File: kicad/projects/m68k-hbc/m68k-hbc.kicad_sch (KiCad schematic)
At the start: 0 parts

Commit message: Modified system architecture, New KiCad Project: Cache Memory Module(SIMM80)
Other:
- removed sheet DMAC
- removed sheet DRAM
- added sheet Clock (Clock.kicad_sch)
- added sheet PBC (PBC.kicad_sch)
- added sheet SYSCON (SYSCON.kicad_sch)
- added sheet USB (USB.kicad_sch)

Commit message: Some Updates
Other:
- sheet EISA renamed ISA
- sheet PBC renamed SBC
- sheet SYSCON renamed CDC
- removed sheet ADDEC
- removed sheet Disk
- removed sheet IO
- removed sheet PIC
- added sheet ATA (ATA.kicad_sch)
- added sheet Config (Config.kicad_sch)
- added sheet DECAP (DECAP.kicad_sch)
- added sheet FDC (FDC.kicad_sch)
- added sheet I2C (I2C.kicad_sch)
- added sheet IO_Timer (IO_Timer.kicad_sch)
- added sheet KeyboardMouse (KeyboardMouse.kicad_sch)
- added sheet OPB (OPB.kicad_sch)
- added sheet PU_PD (PU_PD.kicad_sch)
- added sheet SPI (SPI.kicad_sch)
- sheet Audio ports: added DACK_ACC, DACK_ACP, DRQ_ACC, DRQ_ACP, IRQ_ACODEC, OPB, ~{CS_ACODEC}; removed none
- sheet CDC: file SYSCON.kicad_sch -> CDC.kicad_sch
- sheet CDC ports: added Local Bus, ~{RST_CDC}; removed none
- sheet CPU_FPU ports: added CPUCLK, FPUCLK, Local Bus, ~{CS_FPU}, ~{HLT_CPU}, ~{PRES_FPU}, ~{RST_CPU}, ~{RST_FPU}; removed none
- sheet Clock ports: added CFG_CLK, CLK_24M, CLK_2M, CLK_8M, CLK_CDC, CLK_CPU, CLK_FPU, CLK_ISA, CLK_ISAOSC, CLK_LOCAL, CLK_PEP, CLK_REF, CLK_SBC, System Serial Bus; removed none
- sheet Ethernet ports: added ISA, ISA_IRQ10, ISA_IRQ11, ISA_IRQ12, ISA_IRQ15, ISA_IRQ2, ISA_IRQ3, ISA_IRQ4, ISA_IRQ5, ~{RST_ETH}; removed none
- sheet FWMEM ports: added Local Bus, System Serial Bus, ~{CS_FWM}, ~{CS_NVRAM}; removed none
- sheet ISA: file EISA.kicad_sch -> ISA.kicad_sch
- sheet ISA ports: added CLK_ISA, CLK_ISAOSC, ISA, ISA_IRQ10, ISA_IRQ11, ISA_IRQ12, ISA_IRQ14, ISA_IRQ15, ISA_IRQ2, ISA_IRQ3, ISA_IRQ4, ISA_IRQ5, ISA_IRQ6, ISA_IRQ7, ~{RST_ISA}; removed none
- sheet PEP ports: added CLK_PEP, PEP, System Serial Bus, ~{CERR_P0}, ~{CERR_P1}, ~{CERR_P2}, ~{EN_P0}, ~{EN_P1}, ~{EN_P2}, ~{IRQ_P0}, ~{IRQ_P1}, ~{IRQ_P2}, ~{PRES_P0}, ~{PRES_P1}, ~{PRES_P2}, ~{RST_PEP}; removed none
- sheet Power ports: added PWOK, PWR_FPGA, PWR_PROCESSOR, System Serial Bus, ~{PSON}; removed none
- sheet SBC: file PBC.kicad_sch -> SBC.kicad_sch
- sheet SBC ports: added ATA, ISA, ISA_IRQ10, ISA_IRQ11, ISA_IRQ12, ISA_IRQ14, ISA_IRQ15, ISA_IRQ2, ISA_IRQ3, ISA_IRQ4, ISA_IRQ5, ISA_IRQ6, ISA_IRQ7, Local Bus, OPB, PEP, ~{CERR_P0}, ~{CERR_P1}, ~{CERR_P2}, ~{EN_P0}, ~{EN_P1}, ~{EN_P2}, ~{IRQ_P0}, ~{IRQ_P1}, ~{IRQ_P2}, ~{PRES_P0}, ~{PRES_P1}, ~{PRES_P2}; removed none
- sheet SMC ports: added LED_HDD, OPB, PWOK, SMC_MISO, SMC_MOSI, SMC_RX, SMC_SCK, SMC_SCL, SMC_SDA, SMC_TX, ~{CS_SMC}, ~{IRQ_SMC}, ~{PSON}, ~{RST_SMC}; removed none
- sheet USB ports: added IRQ_USBC, OPB, ~{CS_USBC}, ~{RST_USBC}; removed none

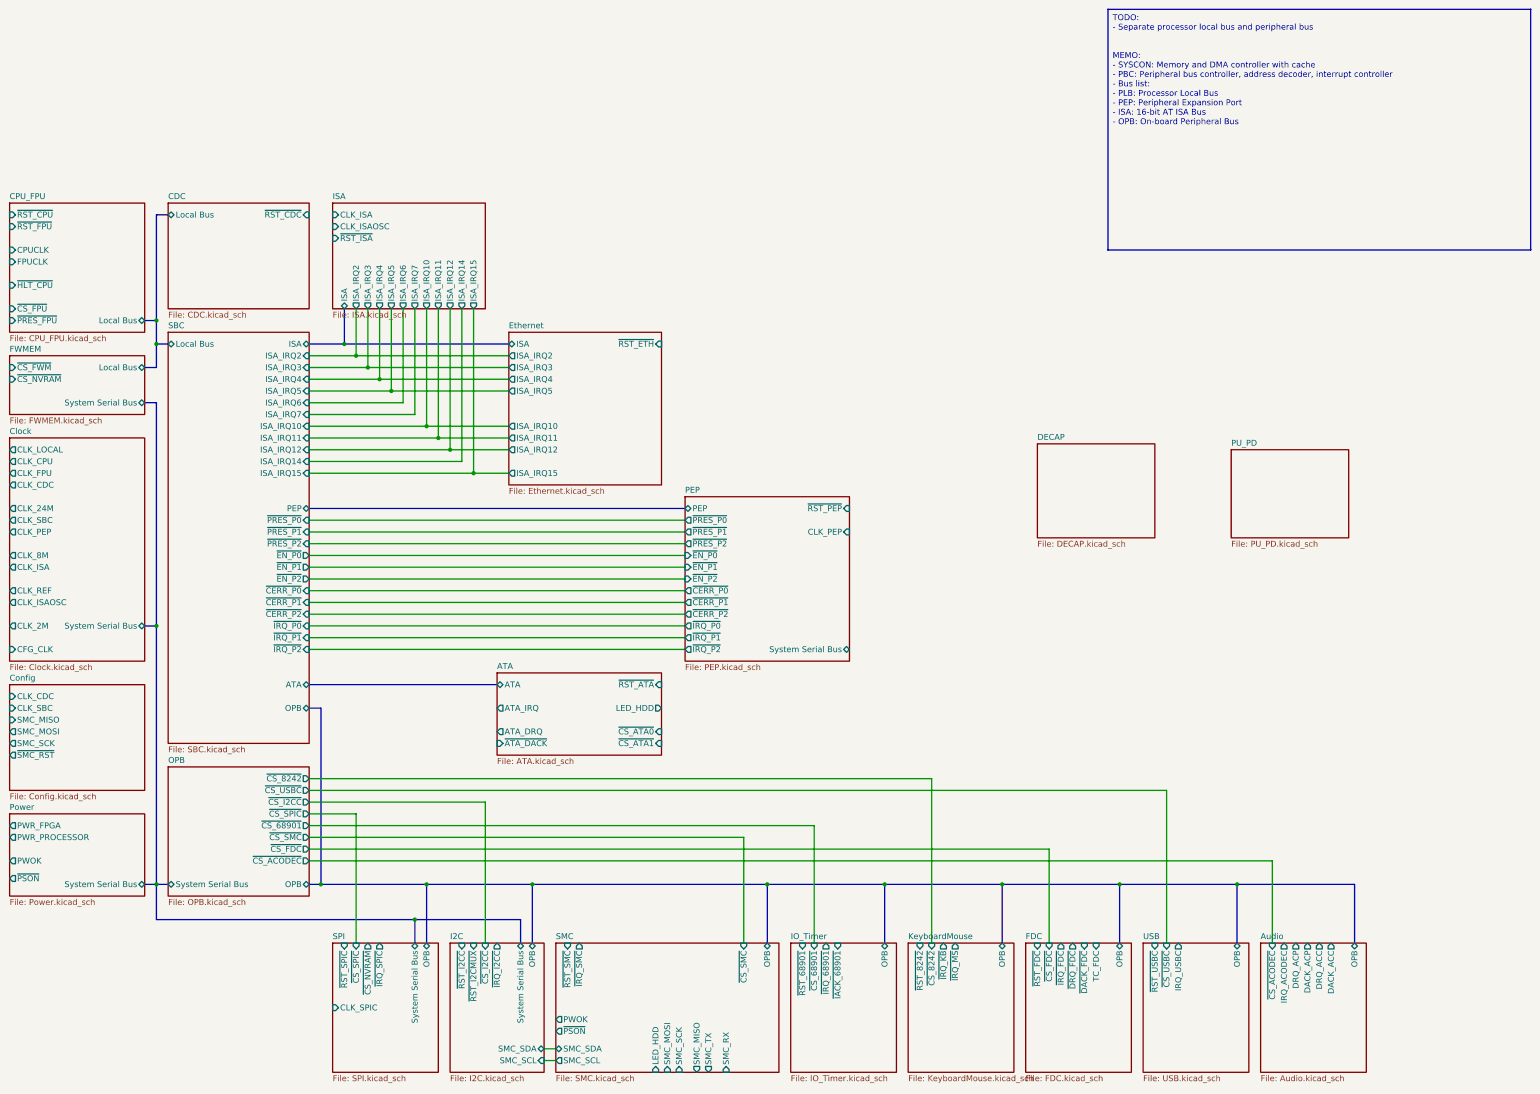
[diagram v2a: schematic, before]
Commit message: Large changes: EHBCSimpleEmu, kicad, fwcode, docs
This commit contains some large changes:
- Removed EHBCSimpleEmu (Moved to kms1212/llemu, kms1212/qemu)
- (likely) Removed fwcode; now it only boots and stops
- Modified documents
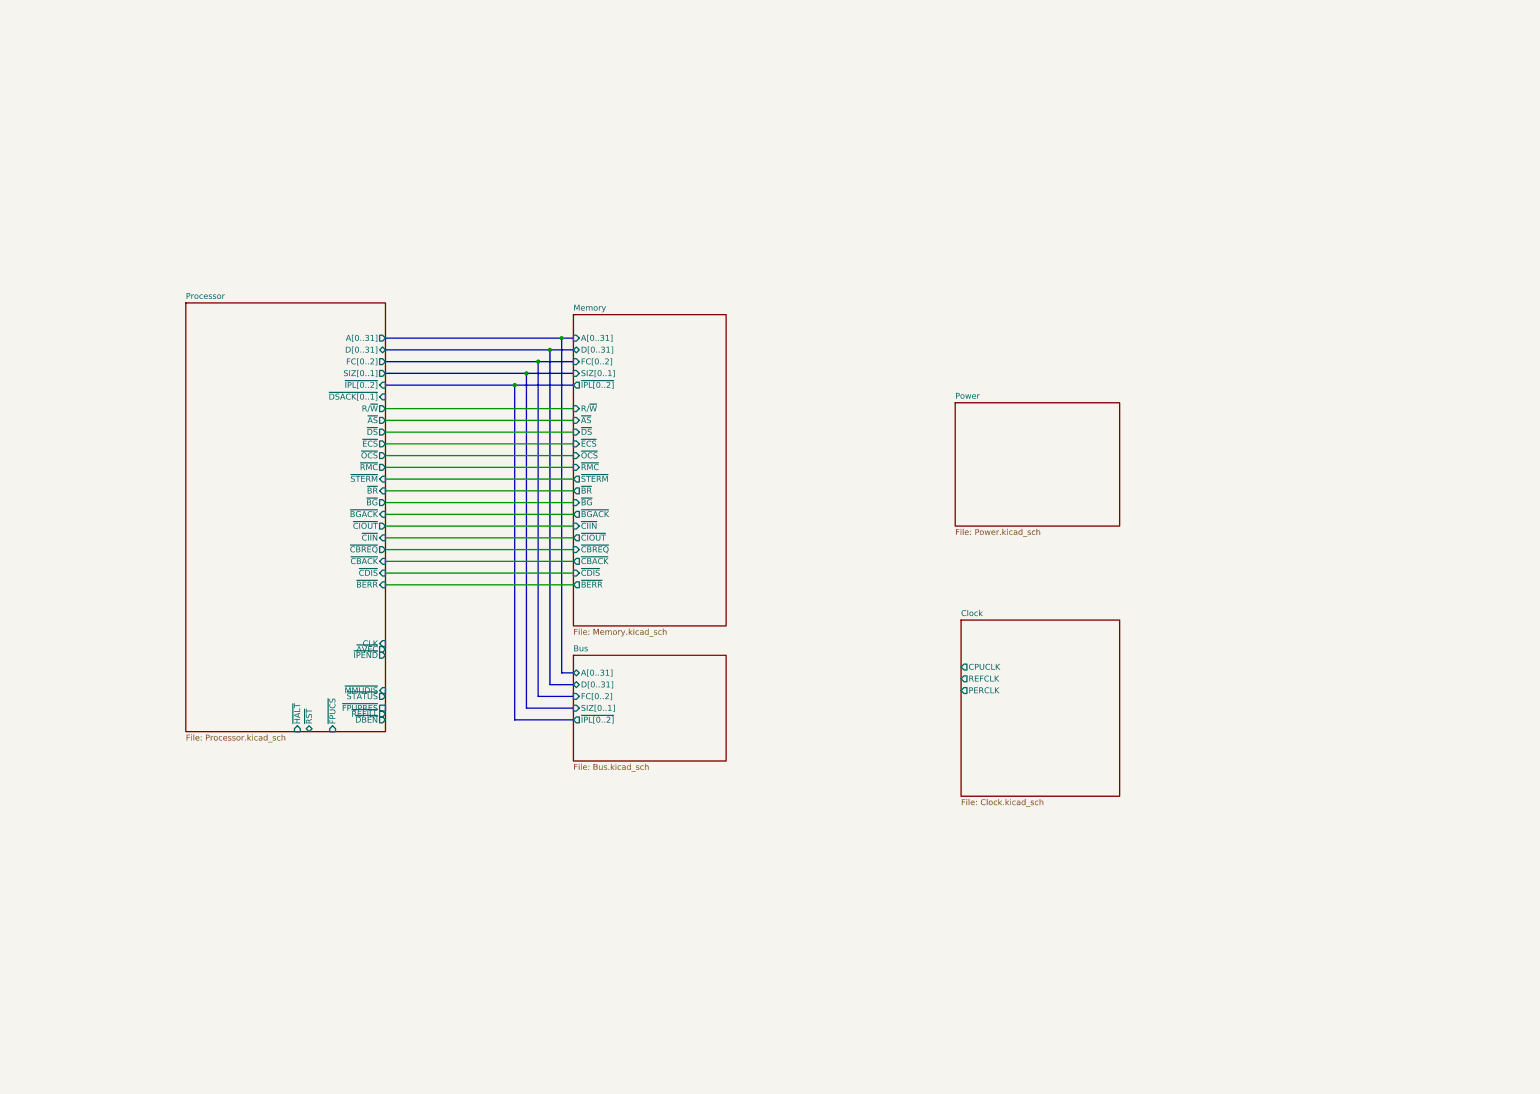
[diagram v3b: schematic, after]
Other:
- removed sheet ATA
- removed sheet Audio
- removed sheet CDC
- removed sheet CPU_FPU
- removed sheet Config
- removed sheet DECAP
- removed sheet Ethernet
- removed sheet FDC
- removed sheet FWMEM
- removed sheet I2C
- removed sheet IO_Timer
- removed sheet ISA
- removed sheet KeyboardMouse
- removed sheet OPB
- removed sheet PEP
- removed sheet PU_PD
- removed sheet SBC
- removed sheet SMC
- removed sheet SPI
- removed sheet USB
- added sheet Bus (Bus.kicad_sch)
- added sheet Memory (Memory.kicad_sch)
- added sheet Processor (Processor.kicad_sch)
- sheet Clock ports: added CPUCLK, PERCLK, REFCLK; removed CFG_CLK, CLK_24M, CLK_2M, CLK_8M, CLK_CDC, CLK_CPU, CLK_FPU, CLK_ISA, CLK_ISAOSC, CLK_LOCAL, CLK_PEP, CLK_REF, CLK_SBC, System Serial Bus
- sheet Power ports: added none; removed PWOK, PWR_FPGA, PWR_PROCESSOR, System Serial Bus, ~{PSON}
- title: (none) -> '030 Extensible Homebrew Computer
